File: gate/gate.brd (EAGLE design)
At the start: 78.7 x 50.5 mm, 25 parts, among them J1 MOLEX_MINILITE_TRAP_2, J2 MOLEX_MINILITE_TRAP_2, J3 MOLEX_MINILITE_TRAP_2, J4 MOLEX_MINILITE_TRAP_2, J5 MOLEX_MINILITE_TRAP_2, J6 MOLEX_MINILITE_TRAP_2, J7 MOLEX_MINILITE_TRAP_2, J8 MOLEX_MINILITE_TRAP_2, J9 MOLEX_MINILITE_TRAP_2, U1 SN75468

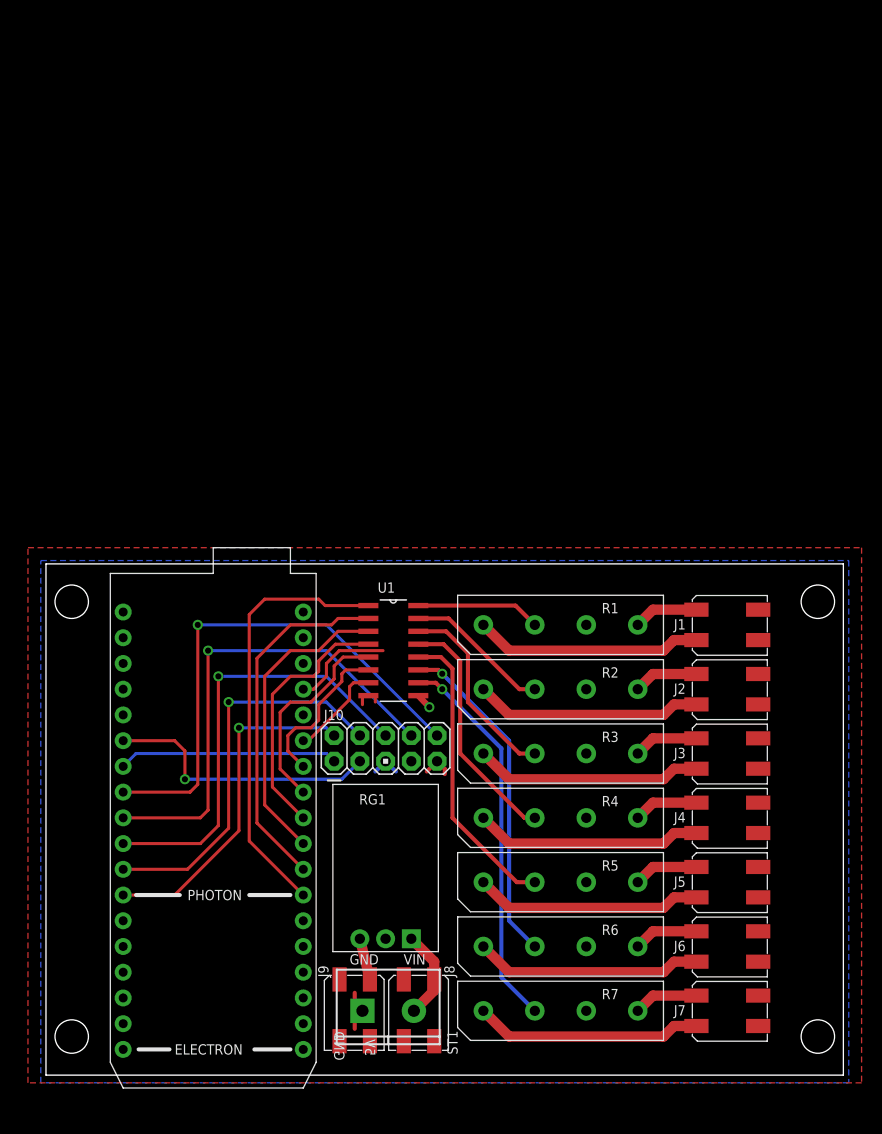
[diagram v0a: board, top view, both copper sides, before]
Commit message: Clean up old files, move gate6 to gate
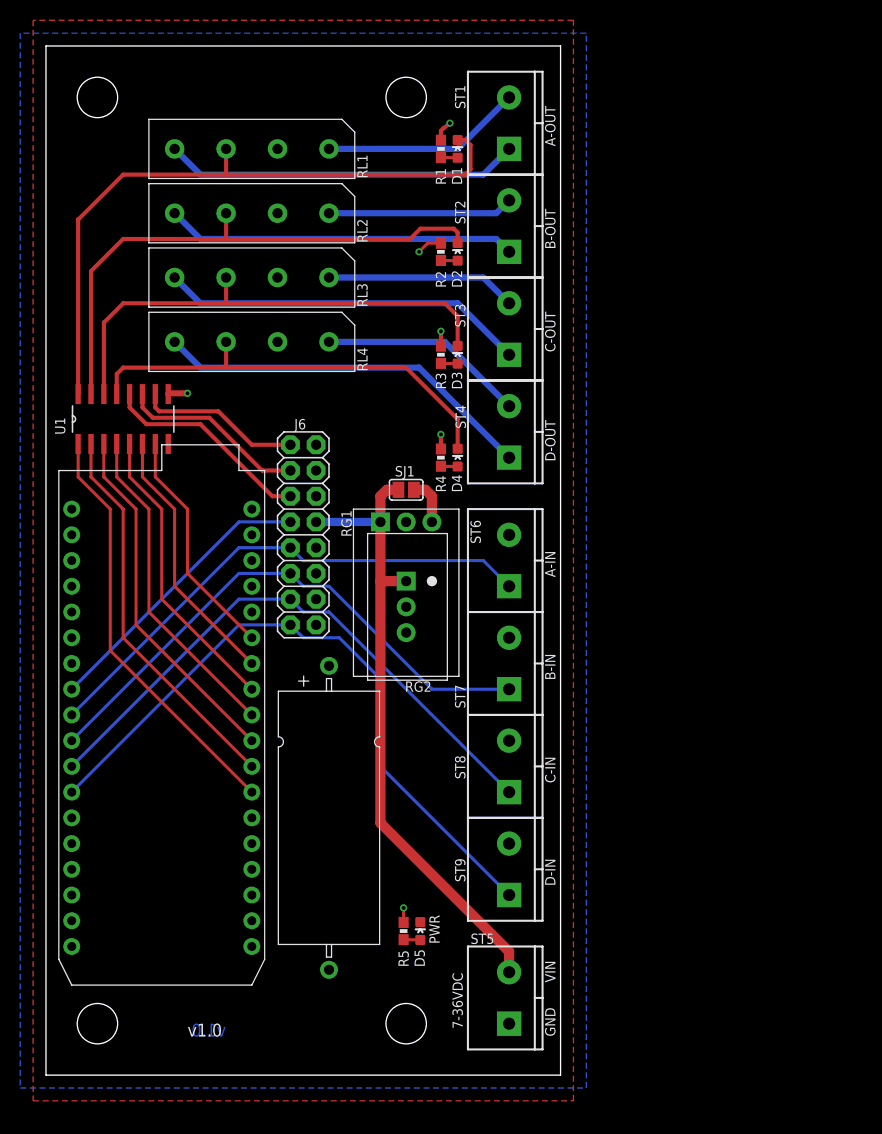
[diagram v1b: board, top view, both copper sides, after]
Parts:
- removed E1: ELECTRON, Puffin:ELECTRON
- removed H1, H2, H3, H4: STAND-OFF, SparkFun-Electromechanical:STAND-OFF
- removed J1, J2, J3, J4, J5, J7, J8, J9: MOLEX_MINILITE_TRAP_2, Puffin:MOLEX_MINILITE_TRAP_2
- removed J10: (no value), SparkFun-Connectors:AVR_ICSP
- removed R6, R7: HE3600_RELAY, Puffin:HE3600_RELAY
- added C1: 470uf, Puffin:CAP-AXIAL-10X25
- added D1, D2, D3, D4, D5: (no value), SparkFun-LED:LED-0603
- added M1: ELECTRON, Puffin:ELECTRON
- added RG2: TRACO_TSR_2, Puffin:TRACO_TSR_2
- added RL1, RL2, RL3, RL4: HE3600_RELAY, Puffin:HE3600_RELAY
- added SJ1: (no value), jumper:SJ
- added ST2, ST3, ST4, ST5, ST6, ST7, ST8, ST9: (no value), Puffin:SCREWTERM_0.2X2
- J6: value MOLEX_MINILITE_TRAP_2 -> (none); device Puffin:MOLEX_MINILITE_TRAP_2 -> SparkFun-Connectors:2X8
- R1, R2, R3, R4, R5: value HE3600_RELAY -> 2.2K; device Puffin:HE3600_RELAY -> SparkFun-Resistors:0603-RES
- moved ST1 86.3 mm to (45.7, 91.4), turned to 90 degrees
- moved J6 65.7 mm to (24.1, 62.2), turned to 270 degrees
- moved R1 47.2 mm to (39.0, 91.4), turned to 270 degrees
- moved R2 43.4 mm to (39.0, 81.3), turned to 270 degrees
- moved RG1 41.2 mm to (35.6, 54.6), turned to 180 degrees
- moved R3 39.6 mm to (39.0, 71.1), turned to 270 degrees
- moved R4 35.8 mm to (39.0, 61.0), turned to 270 degrees
- moved U1 35.1 mm to (7.62, 64.8), turned to 90 degrees
- moved R5 9.24 mm to (35.3, 14.2), turned to 270 degrees
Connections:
- removed net A0: E1.A0, J10.2
- removed net A1: E1.A1, J10.4
- removed net A2: E1.A2, J10.6
- removed net A3: E1.A3, J10.8
- removed net A5: E1.A5, J10.1
- removed net A6: E1.DAC, J10.3
- removed net N$34: R6.2, U1.11
- removed net N$36: J5.1, R5.4
- removed net N$37: J5.2, R5.1
- removed net N$38: J6.1, R6.4
- removed net N$39: J6.2, R6.1
- removed net N$40: J7.1, R7.4
- removed net N$41: J7.2, R7.1
- removed net N$42: E1.D4, U1.5
- removed net N$43: E1.D5, U1.6
- removed net N$44: E1.D6, U1.7
- new net D0: M1.D0, U1.1
- new net D1: M1.D1, U1.2
- new net D2: M1.D2, U1.3
- new net D3: M1.D3, U1.4
- new net D4: M1.D4, U1.5
- new net D5: M1.D5, U1.6
- new net D6: M1.D6, U1.7
- new net L5: J6.5, U1.12
- new net L6: J6.3, U1.11
- new net L7: J6.1, U1.10
- new net N$1: D2.A, R2.2
- new net N$18: J6.9, M1.A3, ST6.1
- new net N$22: D2.C, RL2.3, U1.15
- net 3.3V: now also M1.3V3; no longer E1.3V3
- net 5V: now also C1.+, J6.2, J6.4, J6.6, M1.VIN, R1.1, R2.1, R3.1, R4.1, R5.1, RG2.3, RL1.2, RL2.2, RL3.2, RL4.2, SJ1.2; no longer E1.VIN, J10.5, J9.1, R1.3, R2.3, R3.3, R4.3, R5.3, R6.3, R7.3
- net A4: now also J6.7, M1.A4; no longer E1.A4, J10.10
- net GND: now also C1.-, D5.C, J6.10, J6.12, J6.14, J6.16, M1.GND, M1.GND@2, RG2.2, ST5.1, ST6.2, ST7.2, ST8.2, ST9.2; no longer E1.GND, E1.GND@2, J10.9, J8.2, J9.2, ST1.1
- net N$10: now also RL3.1, ST3.2; no longer J3.1, R3.4
- net N$11: now also RL4.1, ST4.2; no longer J3.2, R3.1
- net N$12: now also RL1.4, ST1.1; no longer J4.1, R4.4
- net N$13: now also RL1.1, ST1.2; no longer J4.2, R4.1
- net N$14: now also D5.A, R5.2; no longer E1.D0, U1.1
- net N$15: now also J6.15, M1.A0, ST9.1; no longer E1.D1, U1.2
- net N$16: now also J6.13, M1.A1, ST8.1; no longer E1.D2, U1.3
- net N$17: now also J6.11, M1.A2, ST7.1; no longer E1.D3, U1.4
- net N$2: now also D4.C, RL4.3, U1.13; no longer R1.2, U1.16
- net N$3: now also D1.A, R1.2; no longer R2.2, U1.15
- net N$33: now also D1.C, RL1.3, U1.16; no longer R5.2, U1.12
- net N$35: now also D3.C, RL3.3, U1.14; no longer R7.2, U1.10
- net N$4: now also D3.A; no longer U1.14
- net N$5: now also D4.A; no longer U1.13
- net N$6: now also RL4.4, ST4.1; no longer J1.1, R1.4
- net N$7: now also RL3.4, ST3.1; no longer J1.2, R1.1
- net N$8: now also RL2.4, ST2.1; no longer J2.1, R2.4
- net N$9: now also RL2.1, ST2.2; no longer J2.2, R2.1
- net VIN: now also J6.8, RG2.1, SJ1.1, ST5.2; no longer J8.1, ST1.2
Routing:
- net VIN: track 8.88 -> 63.2 mm
- net N$22: track 0.00 -> 53.8 mm
- net N$18: track 0.00 -> 51.6 mm
- net A3: track 48.0 -> 0.00 mm, vias 1 -> 0
- net A2: track 43.8 -> 0.00 mm, vias 1 -> 0
- net D0: track 0.00 -> 41.5 mm
- net N$14: track 42.5 -> 1.65 mm
- net A1: track 38.9 -> 0.00 mm, vias 1 -> 0
- net D1: track 0.00 -> 38.4 mm
- net D2: track 0.00 -> 35.3 mm
- net N$33: track 29.3 -> 64.4 mm
- net A0: track 33.9 -> 0.00 mm, vias 1 -> 0
- net N$34: track 33.2 -> 0.00 mm, vias 1 -> 0
- net D3: track 0.00 -> 32.3 mm
- net N$6: track 6.41 -> 37.8 mm
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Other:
- board size 78.7 x 50.5 mm -> 50.8 x 101.6 mm
- board text added: "7-36VDC"
- board text added: "A-IN"
- board text added: "A-OUT"
- board text added: "B-IN"
- board text added: "B-OUT"
- board text added: "C-IN"
- board text added: "C-OUT"
- board text added: "D-IN"
- board text added: "D-OUT"
- board text added: "PWR"
- board text added: "v1.0"
- board text removed: "5V"
- board text removed: "ELECTRON"
- board text removed: "PHOTON"

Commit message: Gate to 2 relays and enclosure fit
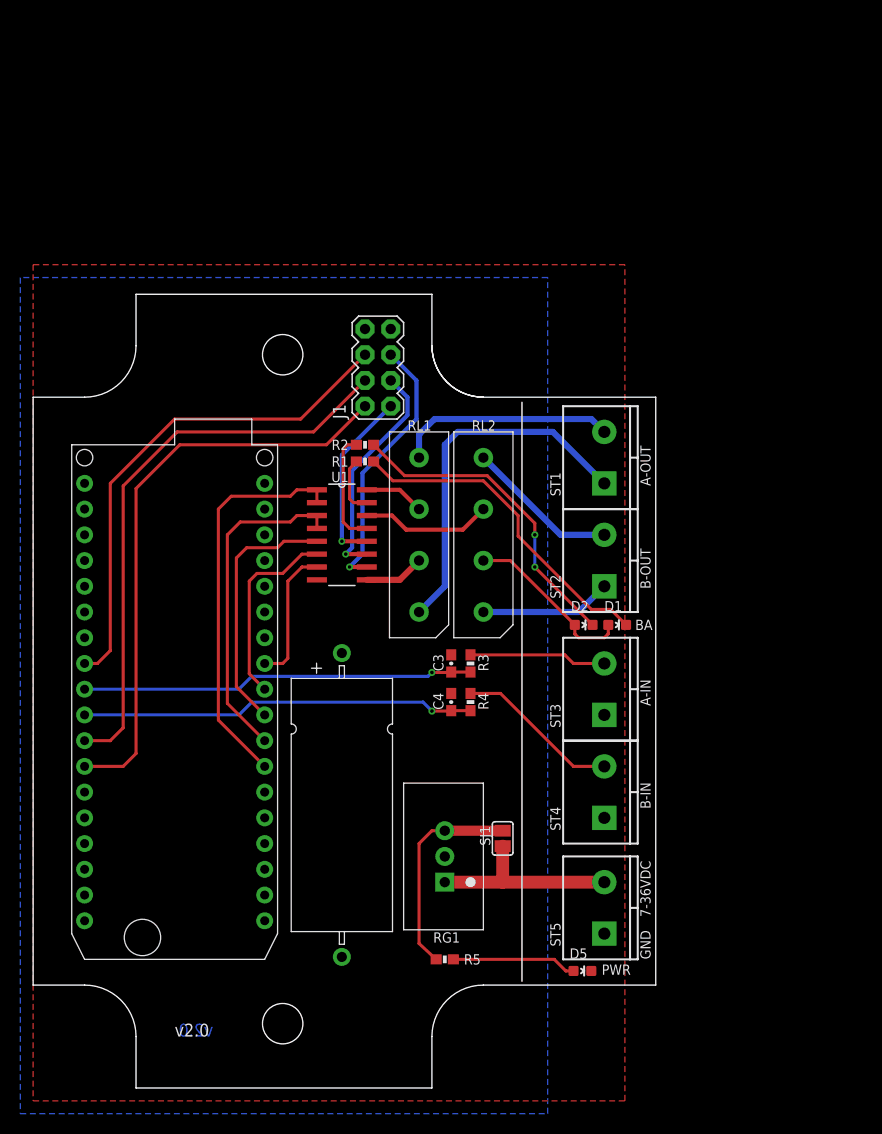
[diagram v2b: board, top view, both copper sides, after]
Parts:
- removed D3, D4: (no value), SparkFun-LED:LED-0603
- removed J6: (no value), SparkFun-Connectors:2X8
- removed RG2: TRACO_TSR_2, Puffin:TRACO_TSR_2
- removed RL3, RL4: HE3600_RELAY, Puffin:HE3600_RELAY
- removed ST6, ST7, ST8, ST9: (no value), Puffin:SCREWTERM_0.2X2
- added C3, C4: .01u, SparkFun-Capacitors:0603-CAP
- added J1: (no value), SparkFun-Connectors:2X4
- R3, R4: value 2.2K -> 1K
- RG1: value (none) -> TRACO_TSR_2; device Puffin:MURATA_REG_HOR -> Puffin:TRACO_TSR_2
- moved D1 49.6 mm to (56.4, 44.5), turned to 270 degrees
- moved RL1 46.6 mm to (36.8, 45.7), turned to 180 degrees
- moved RL2 42.2 mm to (43.2, 45.7), turned to 180 degrees
- moved D2 38.9 mm to (53.1, 44.5), turned to 270 degrees
- moved ST3 36.8 mm to (55.1, 35.6)
- moved ST4 36.8 mm to (55.1, 25.4)
- moved SJ1 35.7 mm to (45.1, 23.4), turned to 90 degrees
- moved ST1 34.3 mm to (55.1, 58.4)
- moved ST2 34.3 mm to (55.1, 48.3)
- moved RG1 33.2 mm to (39.4, 21.6), turned to 90 degrees
- moved R1 31.8 mm to (31.5, 60.6), turned to 180 degrees
- moved R3 30.6 mm to (41.9, 40.6), turned to 90 degrees
- moved U1 24.4 mm to (29.2, 53.3), turned to 0 degrees
- moved R4 24.3 mm to (41.9, 36.8), turned to 90 degrees
- moved R2 20.5 mm to (31.5, 62.2), turned to 180 degrees
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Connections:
- net 3.3V renamed 3V3
- removed net D5: M1.D5, U1.6
- removed net D6: M1.D6, U1.7
- removed net N$10: RL3.1, ST3.2
- removed net N$11: RL4.1, ST4.2
- removed net N$12: RL1.4, ST1.1
- removed net N$15: J6.15, M1.A0, ST9.1
- removed net N$16: J6.13, M1.A1, ST8.1
- removed net N$35: D3.C, RL3.3, U1.14
- new net A0: J1.2, M1.A0
- new net A1: J1.4, M1.A1
- net 5V: now also D1.A, D2.A, J1.8; no longer J6.2, J6.4, J6.6, R1.1, R2.1, R3.1, R4.1, RG2.3, RL3.2, RL4.2
- net A4: now also J1.6; no longer J6.7
- net D0: now also U1.2
- net D1: now also U1.3, U1.4; no longer U1.2
- net D2: now also U1.5; no longer U1.3
- net D3: now also U1.6; no longer U1.4
- net D4: now also U1.7; no longer U1.5
- net GND: now also C3.2, C4.2, J1.7, ST3.1, ST4.1; no longer J6.10, J6.12, J6.14, J6.16, RG2.2, ST6.2, ST7.2, ST8.2, ST9.2
- net L5: now also J1.1; no longer J6.5
- net L6: now also J1.3; no longer J6.3
- net L7: now also J1.5; no longer J6.1
- net N$1: now also D2.C, R2.1; no longer D2.A, R2.2
- net N$13: now also ST1.1; no longer ST1.2
- net N$17: now also R4.2, ST4.2; no longer J6.11, M1.A2, ST7.1
- net N$18: now also R3.2, ST3.2; no longer J6.9, M1.A3, ST6.1
- net N$2: now also RL1.4, ST1.2; no longer D4.C, RL4.3, U1.13
- net N$22: now also U1.14; no longer D2.C, U1.15
- net N$3: now also D1.C, R1.1; no longer D1.A, R1.2
- net N$33: no longer D1.C
- net N$4: now also RL2.4, ST2.2; no longer D3.A, R3.2
- net N$5: now also R2.2, U1.13; no longer D4.A, R4.2
- net N$6: now also R1.2, U1.15; no longer RL4.4, ST4.1
- net N$7: now also C4.1, M1.A2, R4.1; no longer RL3.4, ST3.1
- net N$8: now also C3.1, M1.A3, R3.1; no longer RL2.4, ST2.1
- net N$9: now also ST2.1; no longer ST2.2
- net VIN: no longer J6.8, RG2.1
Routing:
- net N$15: track 66.1 -> 0.00 mm
- net N$33: track 64.4 -> 5.95 mm
- net N$16: track 57.9 -> 0.00 mm
- net A0: track 0.00 -> 57.7 mm
- net A1: track 0.00 -> 56.4 mm
- net N$35: track 48.8 -> 0.00 mm
- net VIN: track 63.2 -> 19.3 mm
- net N$22: track 53.8 -> 12.9 mm
- net N$17: track 54.8 -> 16.2 mm
- net N$18: track 51.6 -> 13.6 mm
- net N$12: track 35.1 -> 0.00 mm
- net N$6: track 37.8 -> 5.81 mm
- net N$3: track 1.65 -> 32.8 mm
- net N$1: track 1.65 -> 31.5 mm, vias 0 -> 2
- net 5V: track 15.5 -> 43.9 mm, vias 6 -> 0
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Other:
- board size 50.8 x 101.6 mm -> 61.5 x 78.4 mm
- board text added: "BA"
- board text added: "v2.0"
- board text removed: "C-IN"
- board text removed: "C-OUT"
- board text removed: "D-IN"
- board text removed: "D-OUT"
- board text removed: "VIN"
- board text removed: "v1.0"

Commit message: Gate: Fix ext header, move pwr led. misc cleanup.
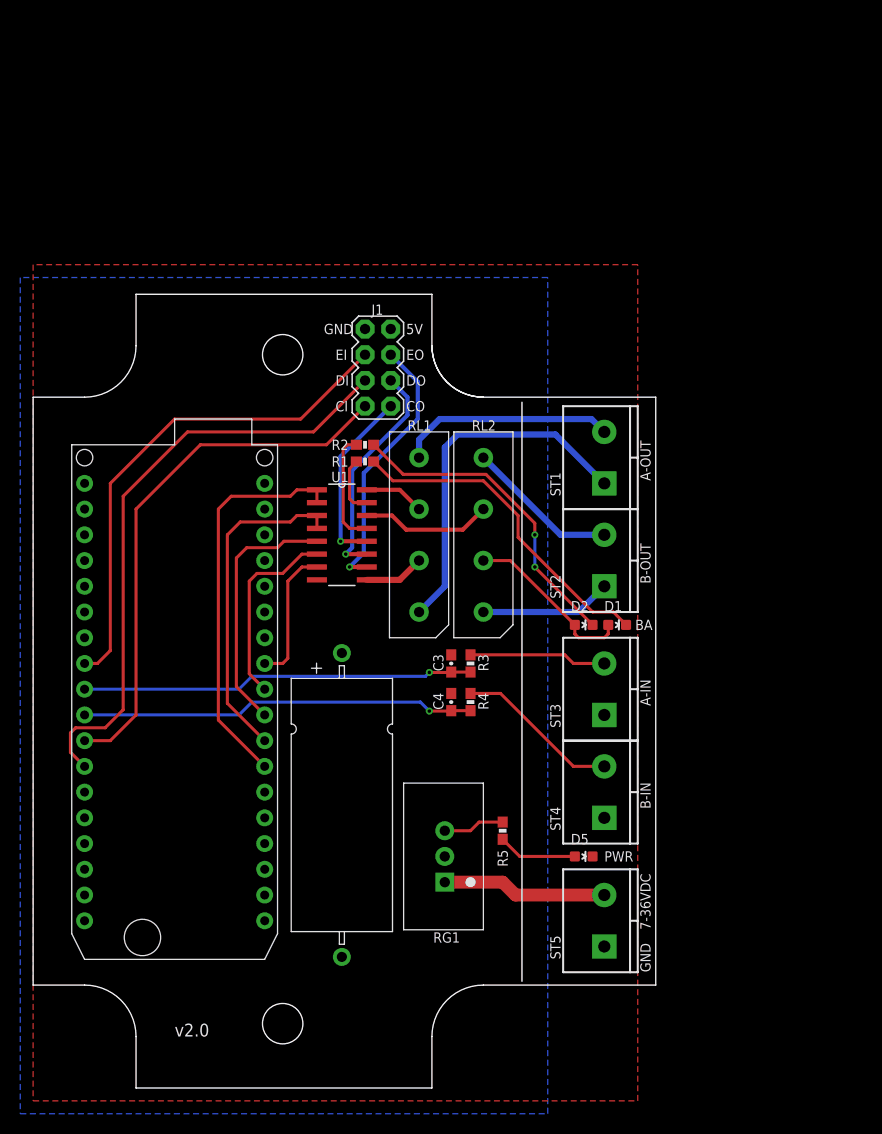
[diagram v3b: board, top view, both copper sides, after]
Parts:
- removed SJ1: (no value), jumper:SJ
- moved R5 13.9 mm to (45.1, 24.1), turned to 270 degrees
- moved D5 11.3 mm to (53.1, 21.6)
- moved ST5 1.27 mm to (55.1, 12.7)
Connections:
- net 5V: now also J1.7; no longer J1.8, SJ1.2
- net A0: now also J1.4; no longer J1.2
- net A1: now also J1.2; no longer J1.4
- net GND: now also J1.8; no longer J1.7
- net VIN: no longer SJ1.1
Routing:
- net 5V: track 43.9 -> 29.1 mm
- net N$14: track 12.3 -> 7.82 mm
- net A1: track 56.4 -> 53.3 mm
- net VIN: track 19.3 -> 16.3 mm
- net A0: track 57.7 -> 59.7 mm
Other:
- board text added: "5V"
- board text added: "CI"
- board text added: "CO"
- board text added: "DI"
- board text added: "DO"
- board text added: "EI"
- board text added: "EO"
